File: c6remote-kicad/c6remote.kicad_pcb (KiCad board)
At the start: 2 copper layers, 37 x 130 mm, 50 parts, among them J1 Battery, Q1 MMBT2222A, Q2 AO3401A, SW1 SW_Push, SW10 SW_Push, SW11 SW_Push, SW2 SW_Push, SW3 SW_Push, SW4 SW_Push, SW5 SW_Push, SW6 SW_Push, SW7 SW_Push, SW8 SW_Push, SW9 SW_Push, U1 XIAO-ESP32-C6, U2 TSOP4136, U3 PCF8575DBR

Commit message: fix(pcb): rotate D5 from 225 to 45 so the four LED ring is actually four-fold symmetric, which it was not: D2, D3 and D4 all sat at consecutive 90 degree steps with VDD facing the wheel centre while D5 was 180 degrees off, pointing VDD outboard, and since a 45 degree multiple rotation swaps DOUT with DIN and VSS with VDD pairwise, that put the incoming led_4 on the pad furthest from D4 and left the D5 corner of the pour carrying both of this rail's earlier copper problems (the 77mm2 orphaned VSS island and the relief starved to one spoke); every pad now faces the same way around the ring, VDD inboard, VSS outboard, DOUT along the chain direction, with nets unmoved on their pin functions (D5 pad 3 DIN on led_4, pad 1 DOUT still the intended no-connect); led_vdd rerouted for the new pad positions, 5 F.Cu segments replacing 2 for 42.6mm F.Cu against 39.3mm before, B.Cu unchanged at 51.9mm and still 4 vias, and the new branch crosses the wheel interior on F.Cu, which is the same move that severed the GND pour neck the first time this rail was routed, but it costs only 2.8mm2 of pour this time and no new island; zones refilled and saved in the GUI, F.Cu GND pour still 2 islands at 2362.1 and 735.9mm2 against 2364.9 and 735.9 before, with all four LED VSS pads verified inside the main island by point-in-polygon rather than by trusting DRC's silence, and the B.Cu +3.3V plane untouched as a single 3348.5mm2 island; DRC 0 errors, 0 unconnected, 43 warnings at the exact inherited breakdown of 24 silk_over_copper, 14 lib_footprint_mismatch, 4 silk_edge_clearance and 1 silk_overlap, parity 13 extra_footprint for the TP_* test points, and the schematic is untouched so ERC is unchanged; kicad_pro came back with its default pad size dropped to 0.5 drill and 1.0 by 1.0, reverted per the repo rule since new-pad defaults are not a design change
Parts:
- turned D5 to 45 degrees
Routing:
- net led_4: track 33.2 -> 29.5 mm
- net led_vdd: track 91.2 -> 94.5 mm
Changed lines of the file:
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@@
 	(footprint "Library:LED_XL-2020RGBC-WS2812B_PLCC4_2.0x2.0mm"
 		(layer "F.Cu")
-		(at 66.8052 81.1818 -135)
+		(at 66.8052 81.1818 45)
 		(descr "XINGLIGHT XL-2020RGBC-WS2812B addressable RGB LED, 2.0x2.0x0.65mm PLCC-4, WS2812B protocol, 5mA/ch, VDD 3.5-5.5V. Land pattern per datasheet recommended soldering pattern: 0.85x0.75mm pads on 1.35x1.25mm centres. Pin 1 DO, 2 GND, 3 DI, 4 VDD. https://mm.digikey.com/Volume0/opasdata/d220001/medias/docus/8903/5962_XL-2020RGBC-WS2812B.pdf")
 		(tags "LED RGB addressable XINGLIGHT XL-2020RGBC WS2812B PLCC-4 2020")
 		(property "Reference" "D5"
-			(at 0 -2.000001 45)
+			(at -0.087257 2.130513 45)
 			(layer "F.SilkS")
 			(effects
@@
 		)
 		(property "Datasheet" "https://mm.digikey.com/Volume0/opasdata/d220001/medias/docus/8903/5962_XL-2020RGBC-WS2812B.pdf"
-			(at 0 0 225)
+			(at 0 0 45)
 			(unlocked yes)
 			(layer "F.Fab")
@@
 		)
 		(property "Description" "RGB LED: XL-2020RGBC-WS2812B addressable, integrated controller, 5mA/ch, VDD 3.5-5.5V, 2020 PLCC4"
-			(at 0 0 225)
+			(at 0 0 45)
 			(unlocked yes)
 			(layer "F.Fab")
@@
 		)
 		(property "Manufacturer" "XINGLIGHT"
-			(at 0 0 225)
+			(at 0 0 45)
 			(unlocked yes)
 			(layer "F.Fab")
@@
 		)
 		(property "MPN" "XL-2020RGBC-WS2812B"
-			(at 0 0 225)
+			(at 0 0 45)
 			(unlocked yes)
 			(layer "F.Fab")
@@
 		)
 		(property "LCSC" "https://www.lcsc.com/product-detail/C5349955.html"
-			(at 0 0 225)
+			(at 0 0 45)
 			(unlocked yes)
 			(layer "F.Fab")
@@
 		)
 		(property "Digikey" "https://www.digikey.com/en/products/detail/xinglight/XL-2020RGBC-WS2812B/25672933"
-			(at 0 0 225)
+			(at 0 0 45)
 			(unlocked yes)
 			(layer "F.Fab")
@@
 		(duplicate_pad_numbers_are_jumpers no)
 		(fp_line
-			(start 1.3 -1.2)
-			(end 1.3 1.2)
+			(start -1 -1.2)
+			(end -1.3 -0.9)
 			(stroke
 				(width 0.12)
-				(type solid)
+				(type default)
 			)
 			(layer "F.SilkS")
 		)
 		(fp_line
-			(start -1.3 1.2)
-			(end 1.3 1.2)
+			(start -1 -1.2)
+			(end 1.3 -1.2)
 			(stroke
 				(width 0.12)
@@
 		)
 		(fp_line
-			(start -1 -1.2)
-			(end 1.3 -1.2)
+			(start -1.3 1.2)
+			(end 1.3 1.2)
 			(stroke
 				(width 0.12)
@@
 		)
 		(fp_line
-			(start -1 -1.2)
-			(end -1.3 -0.9)
+			(start 1.3 -1.2)
+			(end 1.3 1.2)
 			(stroke
 				(width 0.12)
-				(type default)
+				(type solid)
 			)
 			(layer "F.SilkS")
 		)
 		(fp_line
-			(start 1.35 1.25)
-			(end 1.35 -1.25)
+			(start -1.35 -1.25)
+			(end -1.35 1.25)
 			(stroke
 				(width 0.05)
@@
 		)
 		(fp_line
-			(start 1.35 -1.25)
-			(end -1.35 -1.25)
+			(start -1.35 1.25)
+			(end 1.35 1.25)
 			(stroke
 				(width 0.05)
@@
 		)
 		(fp_line
-			(start -1.35 1.25)
-			(end 1.35 1.25)
+			(start 1.35 -1.25)
+			(end -1.35 -1.25)
 			(stroke
 				(width 0.05)
@@
 		)
 		(fp_line
-			(start -1.35 -1.25)
-			(end -1.35 1.25)
+			(start 1.35 1.25)
+			(end 1.35 -1.25)
 			(stroke
 				(width 0.05)
@@
 		)
 		(fp_line
-			(start -1 1)
-			(end 1 1)
+			(start -0.55 -1)
+			(end -1 -0.45)
 			(stroke
 				(width 0.1)
@@
 		)
 		(fp_line
-			(start 1 -1)
-			(end 1 1)
+			(start -1 -0.45)
+			(end -1 1)
 			(stroke
 				(width 0.1)
@@
 		)
 		(fp_line
-			(start -1 -0.45)
-			(end -1 1)
+			(start 1 -1)
+			(end 1 1)
 			(stroke
 				(width 0.1)
@@
 		)
 		(fp_line
-			(start -0.55 -1)
-			(end -1 -0.45)
+			(start -1 1)
+			(end 1 1)
 			(stroke
 				(width 0.1)
@@
 		(fp_poly
 			(pts
-				(xy -0.05 1) (xy -0.5 1) (xy -0.5 0.4) (xy -0.05 0.4)
+				(xy -0.05 -0.45) (xy -0.499999 -0.45) (xy -0.5 -1) (xy -0.05 -1)
 			)
 			(stroke
@@
 		(fp_poly
 			(pts
-				(xy -0.05 -0.45) (xy -0.499999 -0.45) (xy -0.5 -1) (xy -0.05 -1)
+				(xy -0.05 1) (xy -0.5 1) (xy -0.5 0.4) (xy -0.05 0.4)
 			)
 			(stroke
@@
 		)
 		(pad "1" smd rect
-			(at -0.675 -0.625 225)
+			(at -0.675 -0.625 45)
 			(size 0.85 0.75)
 			(layers "F.Cu" "F.Mask" "F.Paste")
@@
 		)
 		(pad "2" smd rect
-			(at -0.675 0.625 225)
+			(at -0.675 0.625 45)
 			(size 0.85 0.75)
 			(layers "F.Cu" "F.Mask" "F.Paste")
@@
 		)
 		(pad "3" smd rect
-			(at 0.675 0.625 225)
+			(at 0.675 0.625 45)
 			(size 0.85 0.75)
 			(layers "F.Cu" "F.Mask" "F.Paste")
@@
 		)
 		(pad "4" smd rect
-			(at 0.675 -0.625 225)
+			(at 0.675 -0.625 45)
 			(size 0.85 0.75)
 			(layers "F.Cu" "F.Mask" "F.Paste")
@@
 	)
 	(segment
-		(start 63.029655 81.217155)
-		(end 65.885961 81.217155)
-		(width 0.2)
-		(layer "F.Cu")
-		(net "led_4")
-	)
-	(segment
 		(start 66.840555 55.165539)
 		(end 66.840555 58.909445)
@@
 	)
 	(segment
-		(start 61 76.5)
-		(end 61 79.1875)
+		(start 64.5 73)
+		(end 68 76.5)
 		(width 0.2)
 		(layer "F.Cu")
@@
 	)
 	(segment
-		(start 66.840555 58.909445)
-		(end 63.25 62.5)
+		(start 68 80.870884)
+		(end 67.724439 81.146445)
 		(width 0.2)
 		(layer "F.Cu")
@@
 	)
 	(segment
-		(start 64.5 73)
-		(end 61 76.5)
+		(start 66.840555 58.909445)
+		(end 63.25 62.5)
 		(width 0.2)
 		(layer "F.Cu")
@@
 	)
 	(segment
-		(start 61 79.1875)
-		(end 63.029655 81.217155)
+		(start 68 76.5)
+		(end 68 80.870884)
 		(width 0.2)
 		(layer "F.Cu")
@@
 	)
 	(segment
+		(start 59.25 71.25)
+		(end 61.25 71.25)
+		(width 0.2)
+		(layer "F.Cu")
+		(net "led_vdd")
+	)
+	(segment
+		(start 54.25 73.25)
+		(end 57.25 73.25)
+		(width 0.2)
+		(layer "F.Cu")
+		(net "led_vdd")
+	)
+	(segment
 		(start 65.460945 54.210945)
 		(end 65.25 54)
@@
 	)
 	(segment
+		(start 57.25 73.25)
+		(end 59.25 71.25)
+		(width 0.2)
+		(layer "F.Cu")
+		(net "led_vdd")
+	)
+	(segment
 		(start 39.5 55.499884)
 		(end 39.834345 55.165539)
@@
 	)
 	(segment
-		(start 42 82.428216)
-		(end 40.788939 81.217155)
+		(start 67.25 79.853116)
+		(end 66.840555 80.262561)
 		(width 0.2)
 		(layer "F.Cu")
@@
 	)
 	(segment
-		(start 54.25 73.25)
-		(end 63.101039 82.101039)
+		(start 67.25 77.25)
+		(end 67.25 79.853116)
+		(width 0.2)
+		(layer "F.Cu")
+		(net "led_vdd")
+	)
+	(segment
+		(start 42 82.428216)
+		(end 40.788939 81.217155)
 		(width 0.2)
 		(layer "F.Cu")
@@
 	)
 	(segment
-		(start 45.5 69.5)
-		(end 45.5 79.489205)
+		(start 61.25 71.25)
+		(end 67.25 77.25)
 		(width 0.2)
 		(layer "F.Cu")
@@
 	)
 	(segment
-		(start 41.217155 81.217155)
-		(end 40.788939 81.217155)
+		(start 45.5 69.5)
+		(end 45.5 79.489205)
 		(width 0.2)
 		(layer "F.Cu")
@@
 	)
 	(segment
-		(start 63.101039 82.101039)
-		(end 66.769845 82.101039)
+		(start 41.217155 81.217155)
+		(end 40.788939 81.217155)
 		(width 0.2)
 		(layer "F.Cu")

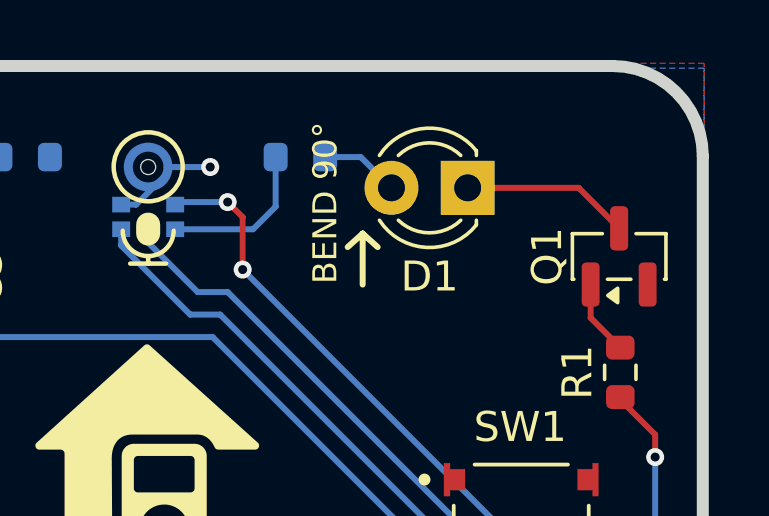
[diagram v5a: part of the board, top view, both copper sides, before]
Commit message: fix(pcb): give D1 a forked horizontal footprint with + and - silk glyphs, since the part is a 3mm IR LED whose leads bend 90 degrees to aim out the top board edge but the board drew it standing upright, and the pad shapes had just been swapped in place so the instance no longer matched LED_THT and DRC sat at 44 warnings; kicad lib/Library.pretty/LED_D3.0mm_Horizontal_O1.27mm_Z2.0mm_IRBlack.kicad_mod forks the stock horizontal variant, which needs no copper change because its pads are the same 1.8mm at (0,0) and (2.54,0), keeps pad 1 circle for the cathode and pad 2 square for the anode as chosen so the square reads as positive, adds 0.9mm + and - glyphs beside the anode and cathode at global (60.2, 30.6) and (65.4, 30.6), and trims the silk body to a base line plus two stubs ending at local y 3.4, which is global 28.875 and 0.66mm clear of the top edge at 28.214, because the real 3mm body overhangs that edge by about 2.6mm and the untrimmed outline would have added silk_edge_clearance violations and been clipped out of the gerbers anyway; the full lying-down body, the dome arc and the courtyard stay on F.Fab and F.CrtYd where no edge rule applies, so the mechanical extent is still documented; the 3D model was already the horizontal Z2.0mm step, so renders and STEP were right while the drawn geometry was wrong, and the two now agree; only the D1 symbol instance carries the new Library: link because editing the schematic's embedded lib_symbols copy raises lib_symbol_mismatch in ERC; zones refilled and saved in the GUI after the pad shape change altered the pour cutouts, F.Cu GND still 2 islands at 2362.8 and 735.9mm2 and the B.Cu +3.3V plane still one at 3348.1mm2; ERC 0, DRC 43 warnings at the inherited breakdown of 24 silk_over_copper, 14 lib_footprint_mismatch, 4 silk_edge_clearance and 1 silk_overlap with D1 no longer among the mismatches, 0 errors, 0 unconnected, parity 13 extra_footprint for the TP_* test points; kicad_pro default pad size drift reverted again
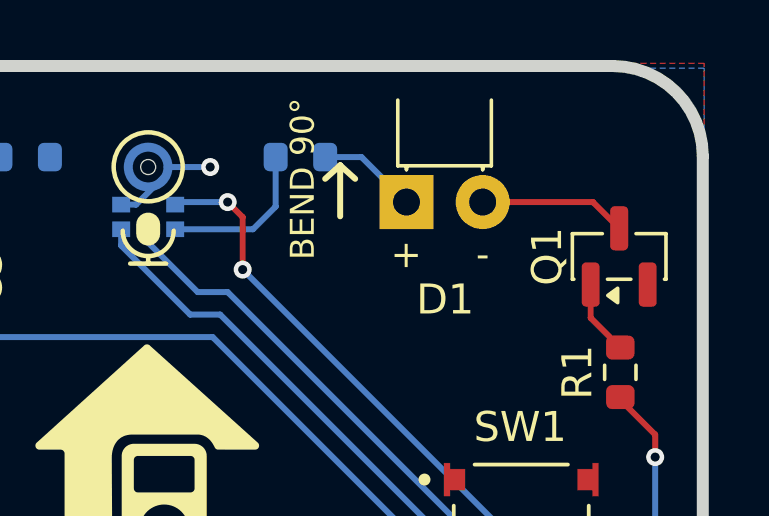
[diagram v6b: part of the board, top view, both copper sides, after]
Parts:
- D1: footprint LED_THT:LED_D3.0mm_IRBlack -> Library:LED_D3.0mm_Horizontal_O1.27mm_Z2.0mm_IRBlack
- moved D1 0.69 mm to (64.5, 32.8)
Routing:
- net Net-(D1-K): track 5.61 -> 4.91 mm
- net Net-(D1-A): track 2.63 -> 3.33 mm
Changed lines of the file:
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@@
 		)
 	)
-	(footprint "LED_THT:LED_D3.0mm_IRBlack"
+	(footprint "Library:LED_D3.0mm_Horizontal_O1.27mm_Z2.0mm_IRBlack"
 		(layer "F.Cu")
-		(at 64 32.275 180)
-		(descr "LED, diameter 3.0mm, 2 pins, infrared, black, generated by kicad-footprint-generator")
+		(at 64.5 32.75 180)
+		(descr "LED, diameter 3.0mm, horizontal offset 1.27mm, z-position of LED center 2.0mm, 2 pins, infrared, black. Fork of LED_THT:LED_D3.0mm_Horizontal_O1.27mm_Z2.0mm_IRBlack for c6remote D1. Pad shapes swapped so the square is pin 2 anode, + and - glyphs added beside the pads, and the silk body outline trimmed to the on-board portion because the real body overhangs the top board edge by about 2.6mm; the full lying-down body stays on F.Fab and F.CrtYd, which carry no edge-clearance rule.")
 		(tags "LED IR")
 		(property "Reference" "D1"
-			(at 1.27 -2.96 0)
+			(at 1.25 -3.25 0)
 			(layer "F.SilkS")
 			(effects
@@
 		)
 		(property "Value" "INL-3AHIR30"
-			(at 5.617455 -0.016 90)
+			(at 0.75 8 180)
 			(layer "F.Fab")
 			(effects
@@
 		(duplicate_pad_numbers_are_jumpers no)
 		(fp_line
-			(start -0.29 1.08)
-			(end -0.29 1.236)
+			(start 2.83 1.21)
+			(end 2.83 3.4)
 			(stroke
 				(width 0.12)
@@
 		)
 		(fp_line
-			(start -0.29 -1.236)
-			(end -0.29 -1.08)
+			(start -0.29 1.21)
+			(end 2.83 1.21)
 			(stroke
 				(width 0.12)
@@
 			(layer "F.SilkS")
 		)
-		(fp_arc
-			(start 2.941437 1.08)
-			(mid 1.36566 1.987699)
-			(end -0.29 1.235516)
-			(stroke
-				(width 0.12)
-				(type solid)
-			)
-			(layer "F.SilkS")
-		)
-		(fp_arc
-			(start 2.310961 1.08)
-			(mid 1.27 1.5)
-			(end 0.229039 1.08)
+		(fp_line
+			(start -0.29 1.21)
+			(end -0.29 3.4)
 			(stroke
 				(width 0.12)
@@
 			(layer "F.SilkS")
 		)
-		(fp_arc
-			(start 0.229039 -1.08)
-			(mid 1.27 -1.5)
-			(end 2.310961 -1.08)
+		(fp_rect
+			(start 2.54 1.08)
+			(end 2.54 1.21)
 			(stroke
 				(width 0.12)
 				(type solid)
 			)
+			(fill no)
 			(layer "F.SilkS")
 		)
-		(fp_arc
-			(start -0.29 -1.235516)
-			(mid 1.36566 -1.987699)
-			(end 2.941437 -1.08)
+		(fp_rect
+			(start 0 1.08)
+			(end 0 1.21)
 			(stroke
 				(width 0.12)
 				(type solid)
 			)
+			(fill no)
 			(layer "F.SilkS")
 		)
 		(fp_rect
-			(start -1.15 -2.21)
-			(end 3.69 2.21)
+			(start -1.21 -1.21)
+			(end 3.75 6.88)
 			(stroke
 				(width 0.05)
@@
 		)
 		(fp_line
-			(start -0.23 -1.16619)
-			(end -0.23 1.16619)
+			(start 2.77 1.27)
+			(end 2.77 5.07)
 			(stroke
 				(width 0.1)
@@
 			(layer "F.Fab")
 		)
-		(fp_arc
-			(start -0.23 -1.16619)
-			(mid 3.17 0)
-			(end -0.23 1.16619)
+		(fp_line
+			(start -0.23 1.27)
+			(end 2.77 1.27)
 			(stroke
 				(width 0.1)
@@
 			(layer "F.Fab")
 		)
-		(fp_circle
-			(center 1.27 0)
-			(end 2.77 0)
+		(fp_line
+			(start -0.23 1.27)
+			(end -0.23 5.07)
+			(stroke
+				(width 0.1)
+				(type solid)
+			)
+			(layer "F.Fab")
+		)
+		(fp_rect
+			(start 2.77 1.27)
+			(end 3.17 2.27)
+			(stroke
+				(width 0.1)
+				(type solid)
+			)
+			(fill no)
+			(layer "F.Fab")
+		)
+		(fp_rect
+			(start 2.54 0)
+			(end 2.54 1.27)
 			(stroke
 				(width 0.1)
@@
 			(layer "F.Fab")
 		)
+		(fp_rect
+			(start 0 0)
+			(end 0 1.27)
+			(stroke
+				(width 0.1)
+				(type solid)
+			)
+			(fill no)
+			(layer "F.Fab")
+		)
+		(fp_arc
+			(start 2.77 5.07)
+			(mid 1.27 6.57)
+			(end -0.23 5.07)
+			(stroke
+				(width 0.1)
+				(type solid)
+			)
+			(layer "F.Fab")
+		)
+		(fp_text user "+"
+			(at 2.55 -1.75 180)
+			(layer "F.SilkS")
+			(effects
+				(font
+					(size 0.9 0.9)
+					(thickness 0.15)
+				)
+			)
+		)
+		(fp_text user "-"
+			(at 0 -1.75 180)
+			(layer "F.SilkS")
+			(effects
+				(font
+					(size 0.9 0.9)
+					(thickness 0.15)
+				)
+			)
+		)
 		(fp_text user "${REFERENCE}"
 			(at 1.27 0 0)
@@
 		)
 		(point
-			(at 62.73 32.275)
+			(at 63.23 27.68)
 			(size 2)
 			(layer "F.Fab")
 		)
-		(pad "1" thru_hole rect
+		(point
+			(at 63.23 32.75)
+			(size 2)
+			(layer "F.Fab")
+		)
+		(pad "1" thru_hole circle
 			(at 0 0 180)
 			(size 1.8 1.8)
@@
 			(pinfunction "K_1")
 			(pintype "passive")
+			(thermal_bridge_angle 90)
 		)
-		(pad "2" thru_hole circle
+		(pad "2" thru_hole rect
 			(at 2.54 0 180)
 			(size 1.8 1.8)
@@
 			(pinfunction "A_2")
 			(pintype "passive")
+			(thermal_bridge_angle 45)
 		)
 		(embedded_fonts no)
@@
 	)
 	(gr_line
-		(start 60.5 33.8)
-		(end 60 34.25)
+		(start 59.75 31.525)
+		(end 59.25 31.975)
 		(stroke
 			(width 0.2)
@@
 	)
 	(gr_line
-		(start 60.5 33.8)
-		(end 61 34.25)
+		(start 59.75 31.525)
+		(end 60.25 31.975)
 		(stroke
 			(width 0.2)
@@
 	)
 	(gr_line
-		(start 60.5 35.5)
-		(end 60.5 33.8)
+		(start 59.75 33.225)
+		(end 59.75 31.525)
 		(stroke
 			(width 0.2)
@@
 	)
 	(gr_text "BEND 90°"
-		(at 59.25 32.775 90)
+		(at 58.5 31.975 90)
 		(layer "F.SilkS")
 		(effects
@@
 	)
 	(segment
-		(start 67.7 32.275)
-		(end 64 32.275)
+		(start 69.05 33.625)
+		(end 68.175 32.75)
 		(width 0.2)
 		(layer "F.Cu")
@@
 	)
 	(segment
-		(start 69.05 33.625)
-		(end 67.7 32.275)
+		(start 68.175 32.75)
+		(end 64.5 32.75)
 		(width 0.2)
 		(layer "F.Cu")
@@
 	)
 	(segment
-		(start 60.435 31.25)
-		(end 59.25 31.25)
+		(start 60.46 31.25)
+		(end 61.96 32.75)
 		(width 0.2)
 		(layer "B.Cu")
@@
 	)
 	(segment
-		(start 60.435 31.25)
-		(end 61.46 32.275)
+		(start 59.25 31.25)
+		(end 60.46 31.25)
 		(width 0.2)
 		(layer "B.Cu")

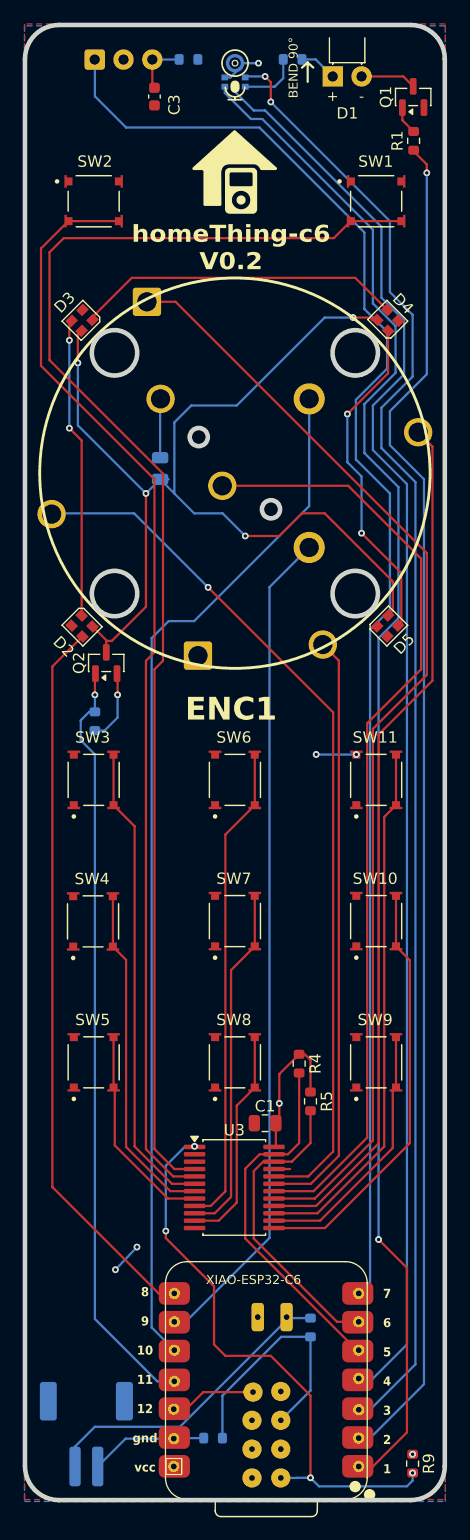
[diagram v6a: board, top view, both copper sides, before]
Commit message: feat(pcb): add three 2.9mm mounting holes for loose M2.5 metal screws into a case, since the board had no fixing points at all and only the four ANO posts and two alignment pegs existed as holes; two flank the top switch row at (39.5, 37.25) and (64.75, 37.25) and one sits on the board axis at (53.337455, 112.95) in the interstice between the SW7 and SW8 rows, drawn as top-level Edge.Cuts gr_circle exactly like the existing ANO 4mm posts and 1.6mm pegs rather than as MountingHole footprints, which keeps them non-plated with no annular ring for a metal screw to short against and adds no BOM line, no c6remote-pos.csv row and no fourteenth extra_footprint parity issue; 2.9mm is the ISO 273 free fit on M2.5, 0.2mm diametral slop to absorb case boss misalignment, and the 0.5mm min_copper_edge_clearance rule carves the pour back on its own, which copper_edge_clearance staying at 0 errors proves; wall clearances are 1.46mm to B.Cu with a 3.21mm FR4 rim at the top left hole, 1.86mm to F.Cu and 2.16mm to D1 at the top right, and 1.11mm to F.Cu with 2.24mm to SW7 at the bottom, so a 5mm pan head fits everywhere but a 6mm washer does not clear R4 at the bottom hole; the bottom hole needed sw6 and sw7 rerouted off the x 52.5 and x 53.0 verticals, 5 F.Cu segments out and 11 in, sw6 detouring left through x 50 for 2.1mm more copper and sw7 right through x 54 to 56 for 0.8mm more, plus the back-silk block opened up, flag and maple leaf up 1.888mm and the OSHW gear and wordmark down 1.503mm, which leaves 1.28mm from the hole wall to the leaf and 1.68mm to the gear where the untouched art had the leaf stem 0.6mm inside the hole and cost a fifth silk_edge_clearance; zones refilled and saved in the GUI, F.Cu GND still 2 islands at 2316.3 and 735.9mm2 and the B.Cu +3.3V plane still one at 3312.2mm2, the three roughly 11.9mm2 losses being the hole voids themselves; schematic untouched so ERC is unchanged, DRC 0 errors, 0 unconnected, 43 warnings at the inherited breakdown of 24 silk_ove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
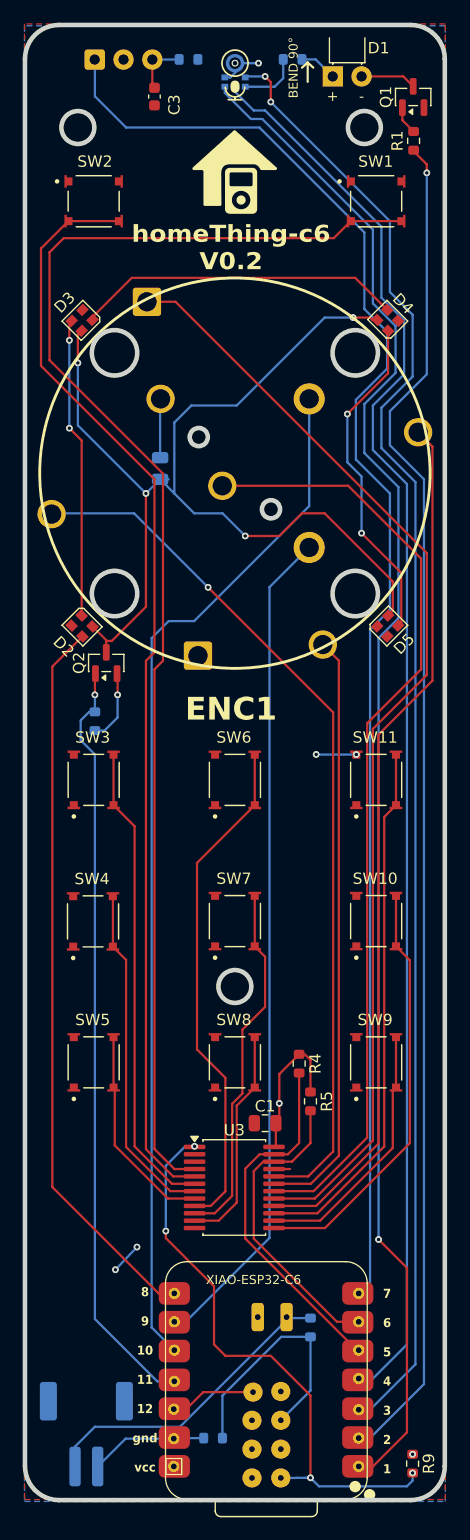
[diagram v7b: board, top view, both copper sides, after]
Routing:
- net sw6: track 42.8 -> 44.9 mm
- net sw7: track 31.2 -> 32.0 mm
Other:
- outline, holes or cut-outs redrawn
